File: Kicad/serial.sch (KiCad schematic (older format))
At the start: 1 part

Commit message: Completed Audio sheet.
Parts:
- gave numbers to parts that had none: 1
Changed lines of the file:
@@
 Sheet 8 9
 Title ""
-Date ""
+Date "2020-12-20"
 Rev ""
-Comp ""
-Comment1 ""
-Comment2 ""
+Comp "https://neotron-compute.github.io/"
+Comment1 "Licenced as CC BY-SA"
+Comment2 "Copyright (c) The Neotron Developers, 2020"
 Comment3 ""
 Comment4 ""
@@
 AR Path="/5FDF5821" Ref="J?"  Part="1"
 AR Path="/5FDEDE75/5FDF5821" Ref="J?"  Part="1"
-F 0 "J?" V 3517 3056 50  0000 C CNN
+AR Path="/5FDF53DB/5FDF5821" Ref="J801"  Part="1"
+F 0 "J801" V 3517 3056 50  0000 C CNN
 F 1 "DB9_Male_MountingHoles" V 3426 3056 50  0000 C CNN
 F 2 "Connector_Dsub:DSUB-9_Male_Horizontal_P2.77x2.84mm_EdgePinOffset4.94mm_Housed_MountingHolesOffset7.48mm" H 3200 3100 50  0001 C CNN

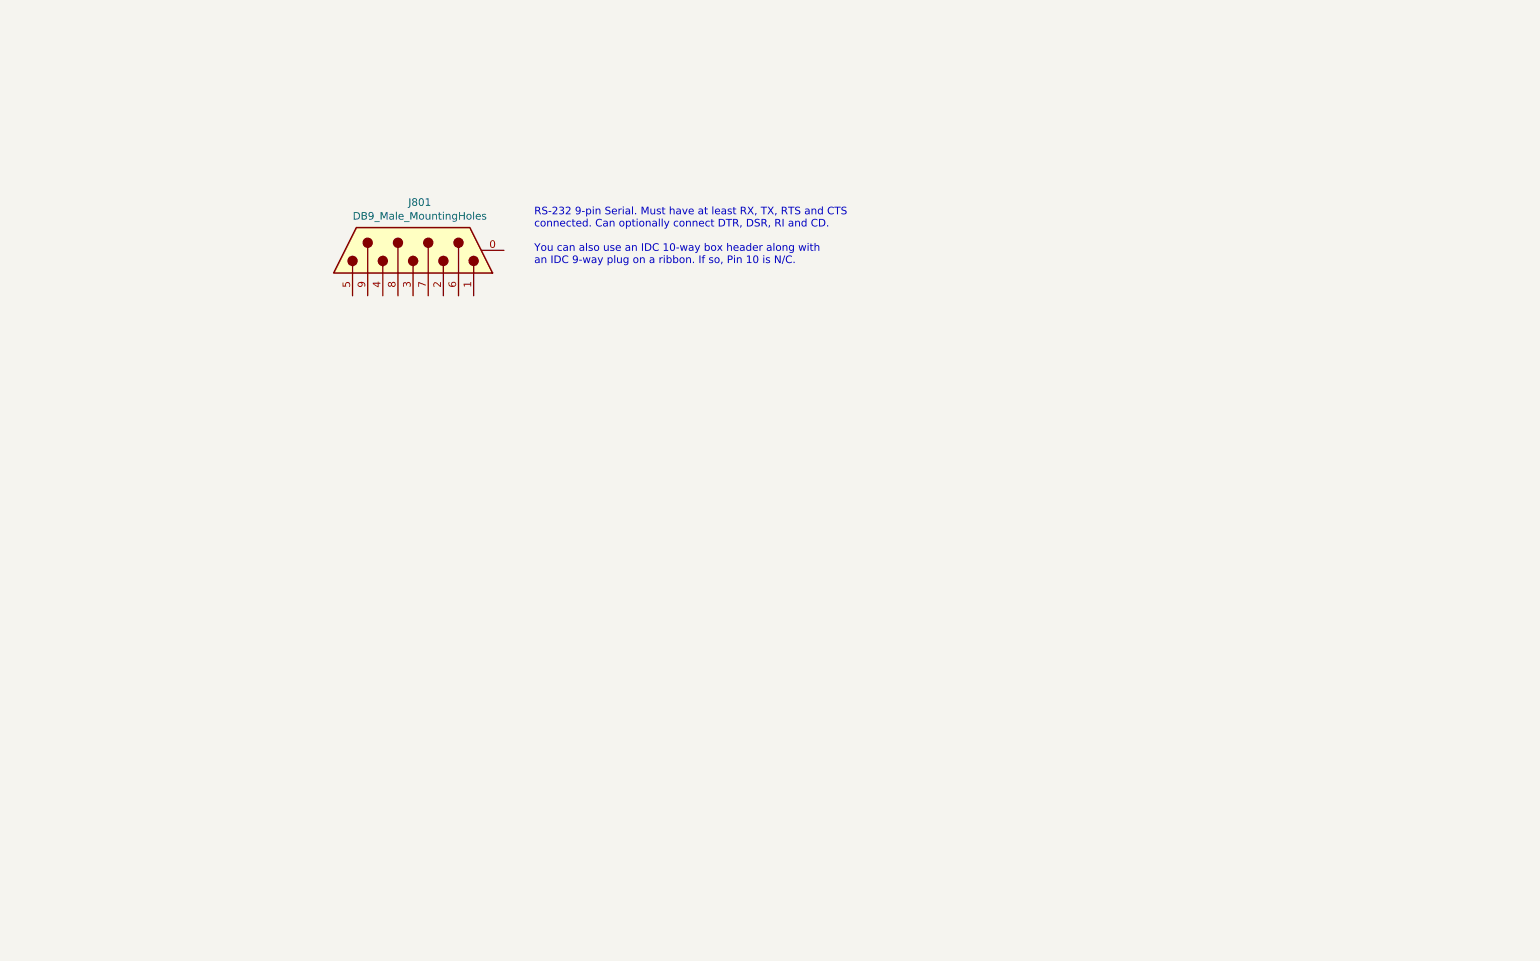
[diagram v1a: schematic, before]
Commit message: Brought in RS232 circuit from Neotron 32.
Also updated 3D models.
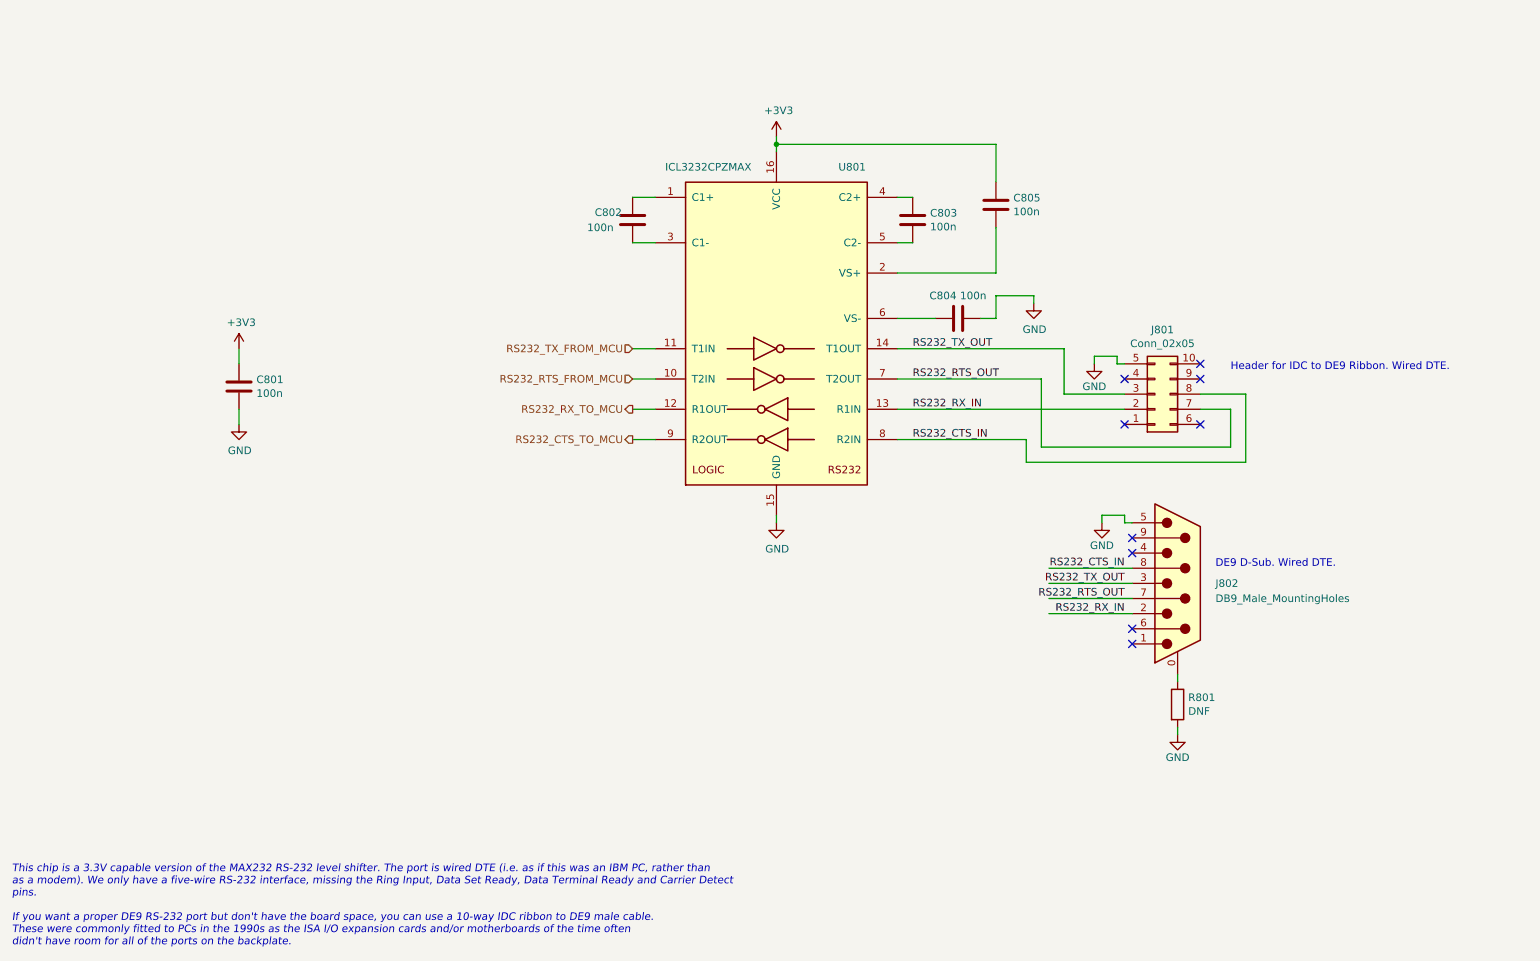
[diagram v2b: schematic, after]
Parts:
- added C801, C802, C803, C804, C805: 100n, Capacitor_THT:C_Disc_D3.0mm_W2.0mm_P2.50mm, symbol Device:C
- added J801: Conn_02x05, Connector_IDC:IDC-Header_2x05_P2.54mm_Vertical, symbol Connector_Generic:Conn_02x05_Top_Bottom
- added R801: DNF, symbol Device:R
- added U801: ICL3232CPZMAX, Package_DIP:DIP-16_W7.62mm, symbol Interface_UART:MAX232
- renumbered J801 to J802
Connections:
- net labels added: +3V3, GND, RS232_CTS_IN, RS232_CTS_TO_MCU, RS232_RTS_FROM_MCU, RS232_RTS_OUT, RS232_RX_IN, RS232_RX_TO_MCU, RS232_TX_FROM_MCU, RS232_TX_OUT
- wire segments 0 -> 50
- no-connect marks 0 -> 9
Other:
- note added: "DE9 D-Sub. Wired DTE."
- note added: "Header for IDC to DE9 Ribbon. Wired DTE."
- note added: "This chip is a 3.3V capable version of the MAX232 RS-232 level shifter. The port is wired DTE (i.e. as if this was an IBM PC, rather than\nas a modem). We only have a five-wire RS-232 interface, missing the Ring Input, Data Set Ready, Data Terminal Ready and Carrier Detect\npins.\n\nIf you want a proper DE9 RS-232 port but don't have the board space, you can use a 10-way IDC ribbon to DE9 male ca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"
- note removed: "RS-232 9-pin Serial. Must have at least RX, TX, RTS and CTS\nconnected. Can optionally connect DTR, DSR, RI and CD.\n\nYou can also use an IDC 10-way box header along with\nan IDC 9-way plug on a ribbon. If so, Pin 10 is N/C."
- moved on the sheet: J802

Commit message: Updating BOM with parts.
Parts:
- C801, C802: Digikey (none) -> BC1150CT-ND
- C803, C804, C805: Digikey (none) -> BC1150CT-ND; mpn K474Z20Y5VE5TL2 -> K104K15X7RF5TL2
- J802: DNP (none) -> 0
- R801: footprint (none) -> Resistor_THT:R_Axial_DIN0207_L6.3mm_D2.5mm_P10.16mm_Horizontal; DNP (none) -> 1
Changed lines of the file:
@@
 F 2 "Connector_Dsub:DSUB-9_Male_Horizontal_P2.77x2.84mm_EdgePinOffset4.94mm_Housed_MountingHolesOffset7.48mm" H 8250 5300 50  0001 C CNN
 F 3 " ~" H 8250 5300 50  0001 C CNN
+F 4 "0" H 8250 5300 50  0001 C CNN "DNP"
 	1    8250 5300
 	1    0    0    -1
@@
 F 3 "~" H 6500 2900 50  0001 C CNN
 F 4 "Vishay" H 0   0   50  0001 C CNN "Manufacturer"
-F 5 "K474Z20Y5VE5TL2" H 0   0   50  0001 C CNN "mpn"
+F 5 "K104K15X7RF5TL2" H 0   0   50  0001 C CNN "mpn"
 F 6 "0" H 6500 2900 50  0001 C CNN "DNP"
+F 7 " BC1150CT-ND" H 6500 2900 50  0001 C CNN "Digikey"
 	1    6500 2900
 	1    0    0    -1
@@
 F 3 "~" H 6800 3550 50  0001 C CNN
 F 4 "Vishay" H 0   0   50  0001 C CNN "Manufacturer"
-F 5 "K474Z20Y5VE5TL2" H 0   0   50  0001 C CNN "mpn"
+F 5 "K104K15X7RF5TL2" H 0   0   50  0001 C CNN "mpn"
 F 6 "0" H 6800 3550 50  0001 C CNN "DNP"
+F 7 " BC1150CT-ND" H 6800 3550 50  0001 C CNN "Digikey"
 	1    6800 3550
 	0    1    1    0
@@
 F 5 "K104K15X7RF5TL2" H 0   0   50  0001 C CNN "mpn"
 F 6 "0" H 4650 2900 50  0001 C CNN "DNP"
+F 7 " BC1150CT-ND" H 4650 2900 50  0001 C CNN "Digikey"
 	1    4650 2900
 	-1   0    0    1
@@
 F 5 "K104K15X7RF5TL2" H -1300 900 50  0001 C CNN "mpn"
 F 6 "0" H 2050 4000 50  0001 C CNN "DNP"
+F 7 " BC1150CT-ND" H 2050 4000 50  0001 C CNN "Digikey"
 	1    2050 4000
 	-1   0    0    1
@@
 F 3 "~" H 7050 2800 50  0001 C CNN
 F 4 "Vishay" H 0   0   50  0001 C CNN "Manufacturer"
-F 5 "K474Z20Y5VE5TL2" H 0   0   50  0001 C CNN "mpn"
+F 5 "K104K15X7RF5TL2" H 0   0   50  0001 C CNN "mpn"
 F 6 "0" H 7050 2800 50  0001 C CNN "DNP"
+F 7 " BC1150CT-ND" H 7050 2800 50  0001 C CNN "Digikey"
 	1    7050 2800
 	1    0    0    -1
@@
 F 0 "R801" H 8320 6146 50  0000 L CNN
 F 1 "DNF" H 8320 6055 50  0000 L CNN
-F 2 "" V 8180 6100 50  0001 C CNN
+F 2 "Resistor_THT:R_Axial_DIN0207_L6.3mm_D2.5mm_P10.16mm_Horizontal" V 8180 6100 50  0001 C CNN
 F 3 "~" H 8250 6100 50  0001 C CNN
+F 4 "1" H 8250 6100 50  0001 C CNN "DNP"
 	1    8250 6100
 	1    0    0    -1

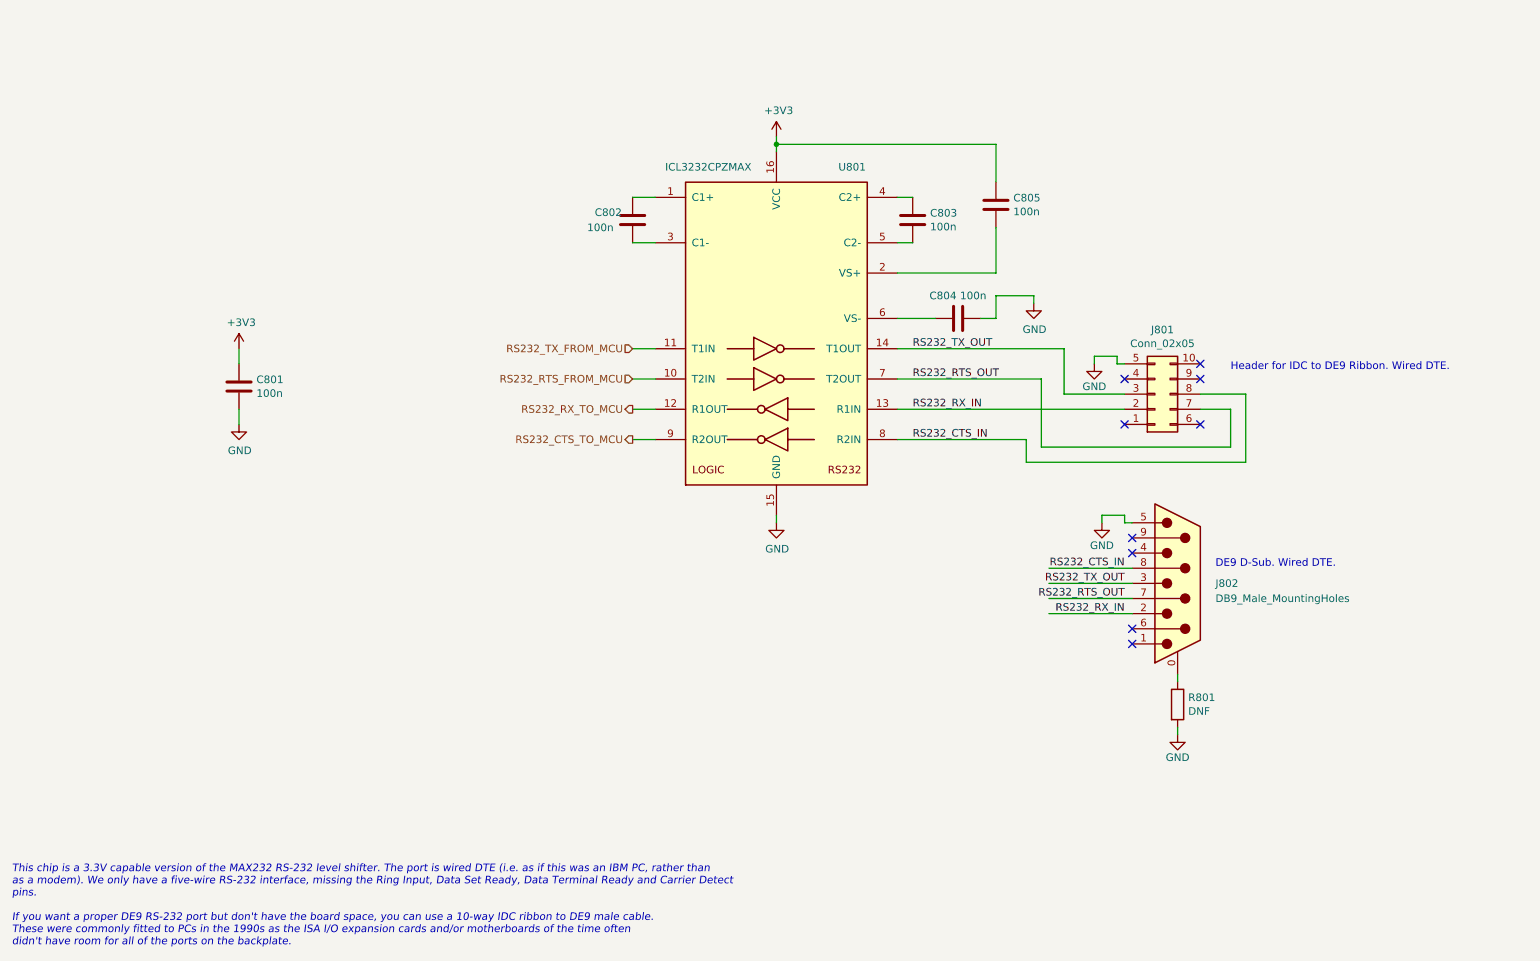
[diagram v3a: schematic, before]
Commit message: Gave sheets unique titles
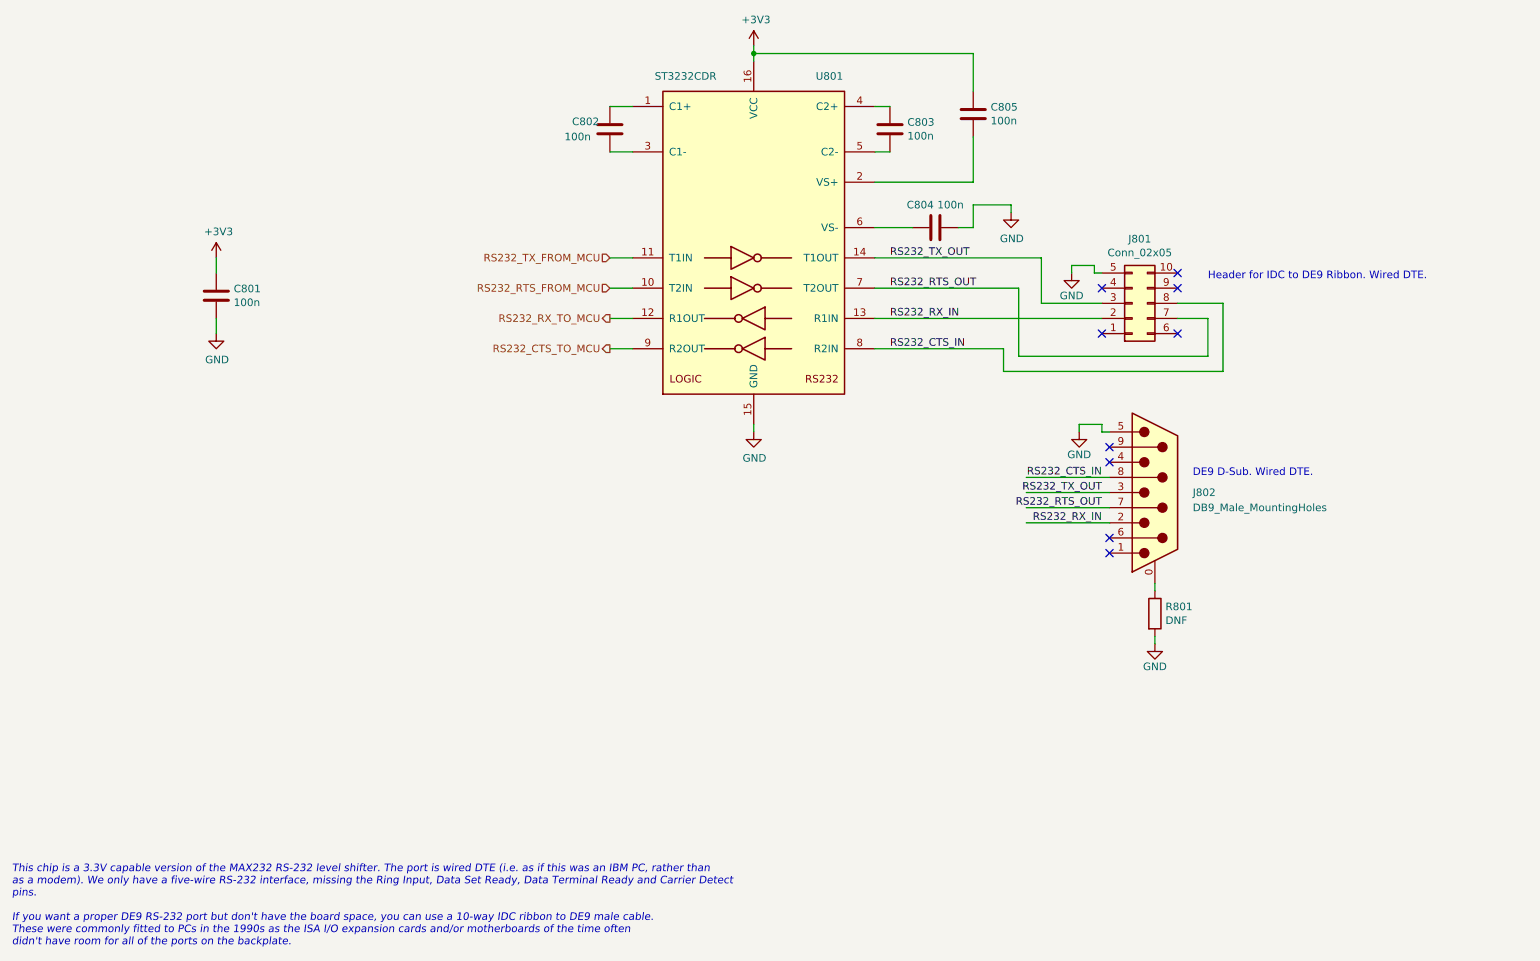
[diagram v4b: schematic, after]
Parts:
- C801, C802, C803, C804, C805: footprint Capacitor_THT:C_Disc_D3.0mm_W2.0mm_P2.50mm -> Capacitor_SMD:C_0805_2012Metric_Pad1.15x1.40mm_HandSolder
- R801: footprint Resistor_THT:R_Axial_DIN0207_L6.3mm_D2.5mm_P10.16mm_Horizontal -> Resistor_SMD:R_0805_2012Metric_Pad1.15x1.40mm_HandSolder
- U801: value ICL3232CPZMAX -> ST3232CDR; footprint Package_DIP:DIP-16_W7.62mm -> Package_SO:SOP-16_4.4x10.4mm_P1.27mm; Manufacturer Renesas;On Shore Technology -> ST; mpn ICL3232CPZ;ED16DT -> ST3232CDR
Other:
- moved on the sheet: C801, C802, C803, C804, C805, J801, J802, R801, U801
